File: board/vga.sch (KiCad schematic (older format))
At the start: 19 parts, among them P601 3-RCA

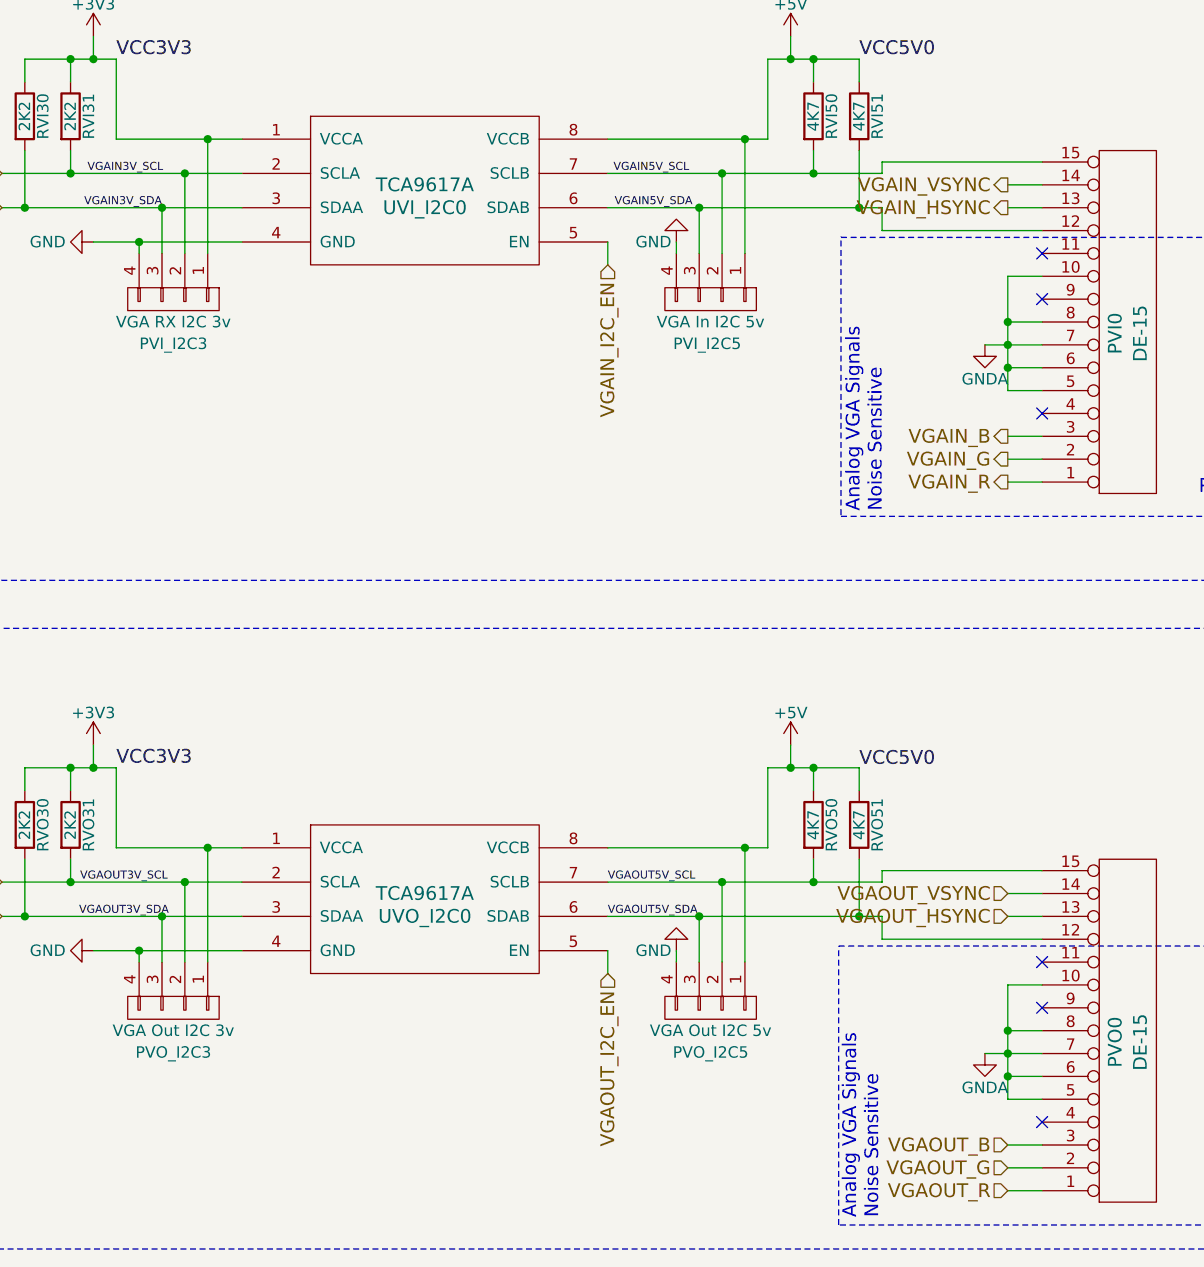
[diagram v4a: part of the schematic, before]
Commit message: Moving I2C enable pins to make IO1 a NC.
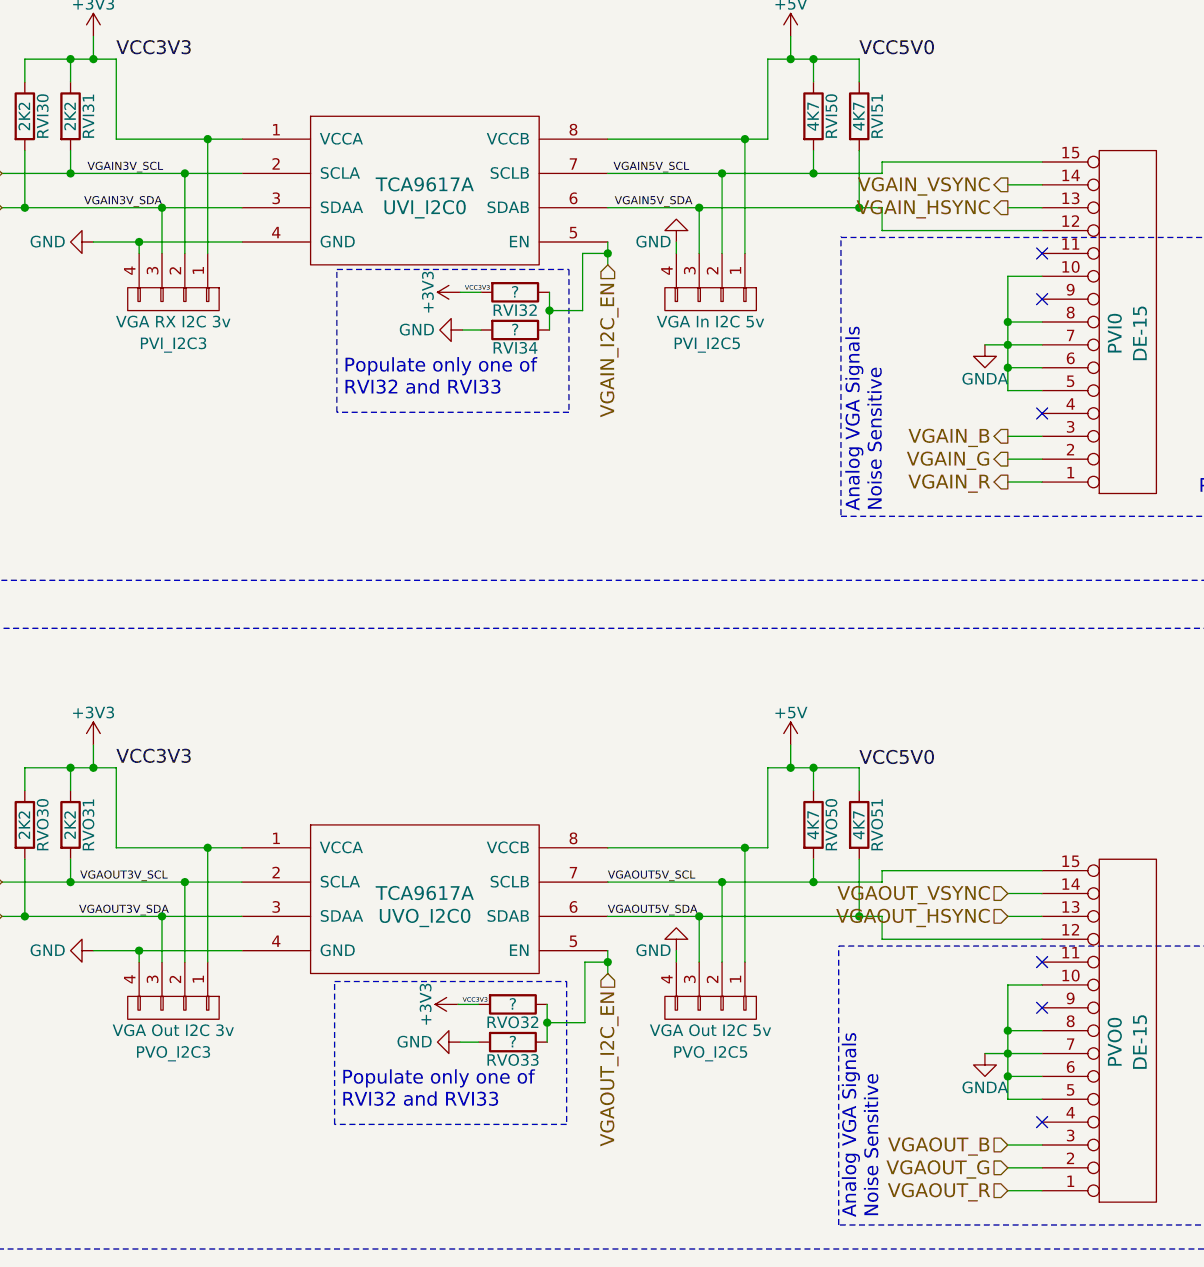
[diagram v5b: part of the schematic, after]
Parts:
- added RVI32, RVI34, RVO32, RVO33: ?, Resistors_SMD:R_0805_HandSoldering, symbol R
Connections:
- net +3V3: now also RVI32.2, RVO32.2
- net GND: now also RVI34.2, RVO33.2
- net VGAIN_I2C_EN: now also RVI32.1, RVI34.1
- net VGAOUT_I2C_EN: now also RVO32.1, RVO33.1
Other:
- note added: "Populate only one of \nRVI32 and RVI33"
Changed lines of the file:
@@
 Connection ~ 4600 5050
 Wire Wire Line
-	4600 5250 4600 5050
+	4600 5050 4600 5250
 Connection ~ 4700 4900
 Wire Wire Line
-	4700 5250 4700 4900
+	4700 4900 4700 5250
 Connection ~ 4800 4750
 Wire Wire Line
@@
 Connection ~ 4600 1950
 Wire Wire Line
-	4600 2150 4600 1950
+	4600 1950 4600 2150
 Connection ~ 4700 1800
 Wire Wire Line
-	4700 2150 4700 1800
+	4700 1800 4700 2150
 Connection ~ 4800 1650
 Wire Wire Line
@@
 	7650 1700 7650 1950
 Wire Wire Line
-	7750 1950 6550 1950
-Wire Wire Line
-	7750 1800 6550 1800
+	6550 1950 7750 1950
+Wire Wire Line
+	6550 1800 7750 1800
 Connection ~ 4000 1950
 Wire Wire Line
@@
 	4200 1400 4200 1300
 Wire Wire Line
-	7750 2050 7750 1950
-Wire Wire Line
-	7750 1750 7750 1800
+	7750 1950 7750 2050
+Wire Wire Line
+	7750 1800 7750 1750
 Connection ~ 8300 2450
 Connection ~ 8300 2650
@@
 	8300 2250 8300 2750
 Wire Wire Line
-	8450 2050 7750 2050
-Wire Wire Line
-	8450 1750 7750 1750
+	7750 2050 8450 2050
+Wire Wire Line
+	7750 1750 8450 1750
 Wire Wire Line
 	8450 2250 8300 2250
@@
 	7650 4800 7650 5050
 Wire Wire Line
-	7750 5050 6550 5050
-Wire Wire Line
-	7750 4900 6550 4900
+	6550 5050 7750 5050
+Wire Wire Line
+	6550 4900 7750 4900
 Connection ~ 4000 5050
 Wire Wire Line
@@
 	4200 4500 4200 4400
 Wire Wire Line
-	7750 5150 7750 5050
-Wire Wire Line
-	7750 4850 7750 4900
+	7750 5050 7750 5150
+Wire Wire Line
+	7750 4900 7750 4850
 Connection ~ 8300 5550
 Connection ~ 8300 5750
@@
 	8300 5350 8300 5850
 Wire Wire Line
-	8450 5150 7750 5150
-Wire Wire Line
-	8450 4850 7750 4850
+	7750 5150 8450 5150
+Wire Wire Line
+	7750 4850 8450 4850
 Wire Wire Line
 	8450 5350 8300 5350
@@
 Wire Notes Line
 	2755 2600 740  2600
+$Comp
+L R RVI32
+U 1 1 57A40937
+P 6145 2320
+F 0 "RVI32" V 6225 2320 50  0000 C CNN
+F 1 "?" V 6145 2320 50  0000 C CNN
+F 2 "Resistors_SMD:R_0805_HandSoldering" V 6075 2320 30  0001 C CNN
+F 3 "" H 6145 2320 30  0000 C CNN
+	1    6145 2320
+	0    1    1    0
+$EndComp
+$Comp
+L R RVI34
+U 1 1 57A40A93
+P 6145 2485
+F 0 "RVI34" V 6225 2485 50  0000 C CNN
+F 1 "?" V 6145 2485 50  0000 C CNN
+F 2 "Resistors_SMD:R_0805_HandSoldering" V 6075 2485 30  0001 C CNN
+F 3 "" H 6145 2485 30  0000 C CNN
+	1    6145 2485
+	0    1    1    0
+$EndComp
+Wire Wire Line
+	6295 2320 6295 2485
+Wire Wire Line
+	6295 2400 6440 2400
+Wire Wire Line
+	6440 2400 6440 2150
+Wire Wire Line
+	6440 2150 6550 2150
+Connection ~ 6550 2150
+Connection ~ 6295 2400
+$Comp
+L +3V3 #PWR?
+U 1 1 57A40F97
+P 5905 2320
+F 0 "#PWR?" H 5905 2170 50  0001 C CNN
+F 1 "+3V3" H 5905 2460 50  0000 C CNN
+F 2 "" H 5905 2320 60  0000 C CNN
+F 3 "" H 5905 2320 60  0000 C CNN
+	1    5905 2320
+	0    -1   -1   0
+$EndComp
+Text Label 5925 2320 0    20   ~ 0
+VCC3V3
+$Comp
+L GND #PWR?
+U 1 1 57A411C9
+P 5915 2485
+F 0 "#PWR?" H 5915 2235 50  0001 C CNN
+F 1 "GND" V 5915 2285 50  0000 C CNN
+F 2 "" H 5915 2485 60  0000 C CNN
+F 3 "" H 5915 2485 60  0000 C CNN
+	1    5915 2485
+	0    1    -1   0
+$EndComp
+Wire Wire Line
+	5995 2485 5915 2485
+Wire Wire Line
+	5905 2320 5995 2320
+Text Notes 5395 2780 0    60   ~ 0
+Populate only one of \nRVI32 and RVI33
+Wire Notes Line
+	5365 2220 6380 2220
+Wire Notes Line
+	6380 2220 6380 2845
+Wire Notes Line
+	6380 2845 5365 2845
+Wire Notes Line
+	5365 2845 5365 2230
+$Comp
+L R RVO32
+U 1 1 57A419BF
+P 6135 5435
+F 0 "RVO32" V 6215 5435 50  0000 C CNN
+F 1 "?" V 6135 5435 50  0000 C CNN
+F 2 "Resistors_SMD:R_0805_HandSoldering" V 6065 5435 30  0001 C CNN
+F 3 "" H 6135 5435 30  0000 C CNN
+	1    6135 5435
+	0    1    1    0
+$EndComp
+$Comp
+L R RVO33
+U 1 1 57A419C5
+P 6135 5600
+F 0 "RVO33" V 6215 5600 50  0000 C CNN
+F 1 "?" V 6135 5600 50  0000 C CNN
+F 2 "Resistors_SMD:R_0805_HandSoldering" V 6065 5600 30  0001 C CNN
+F 3 "" H 6135 5600 30  0000 C CNN
+	1    6135 5600
+	0    1    1    0
+$EndComp
+Wire Wire Line
+	6285 5435 6285 5600
+Wire Wire Line
+	6285 5515 6450 5515
+Connection ~ 6285 5515
+$Comp
+L +3V3 #PWR?
+U 1 1 57A419CF
+P 5895 5435
+F 0 "#PWR?" H 5895 5285 50  0001 C CNN
+F 1 "+3V3" H 5895 5575 50  0000 C CNN
+F 2 "" H 5895 5435 60  0000 C CNN
+F 3 "" H 5895 5435 60  0000 C CNN
+	1    5895 5435
+	0    -1   -1   0
+$EndComp
+Text Label 5915 5435 0    20   ~ 0
+VCC3V3
+$Comp
+L GND #PWR?
+U 1 1 57A419D6
+P 5905 5600
+F 0 "#PWR?" H 5905 5350 50  0001 C CNN
+F 1 "GND" V 5905 5400 50  0000 C CNN
+F 2 "" H 5905 5600 60  0000 C CNN
+F 3 "" H 5905 5600 60  0000 C CNN
+	1    5905 5600
+	0    1    -1   0
+$EndComp
+Wire Wire Line
+	5985 5600 5905 5600
+Wire Wire Line
+	5895 5435 5985 5435
+Text Notes 5385 5895 0    60   ~ 0
+Populate only one of \nRVI32 and RVI33
+Wire Notes Line
+	5355 5335 6370 5335
+Wire Notes Line
+	6370 5335 6370 5960
+Wire Notes Line
+	6370 5960 5355 5960
+Wire Notes Line
+	5355 5960 5355 5345
+Wire Wire Line
+	6450 5515 6450 5250
+Wire Wire Line
+	6450 5250 6550 5250
+Connection ~ 6550 5250
 $EndSCHEMATC

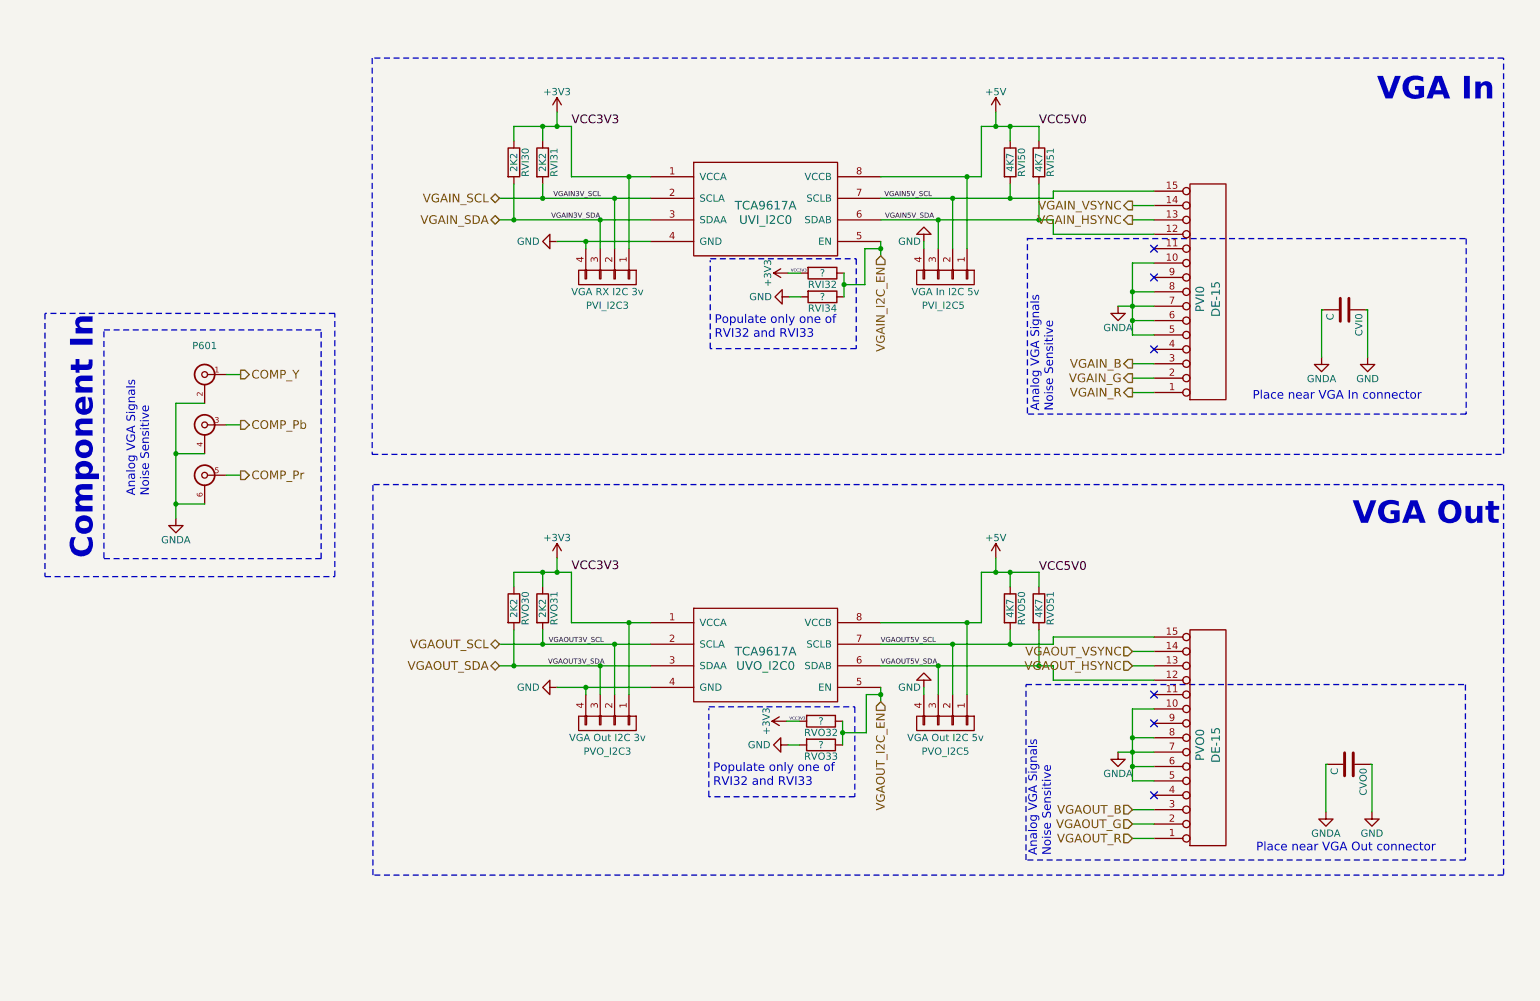
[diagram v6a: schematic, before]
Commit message: Added ESD protection to video inputs Changed level shifter to TPSDS019 because it also contains ESD protection
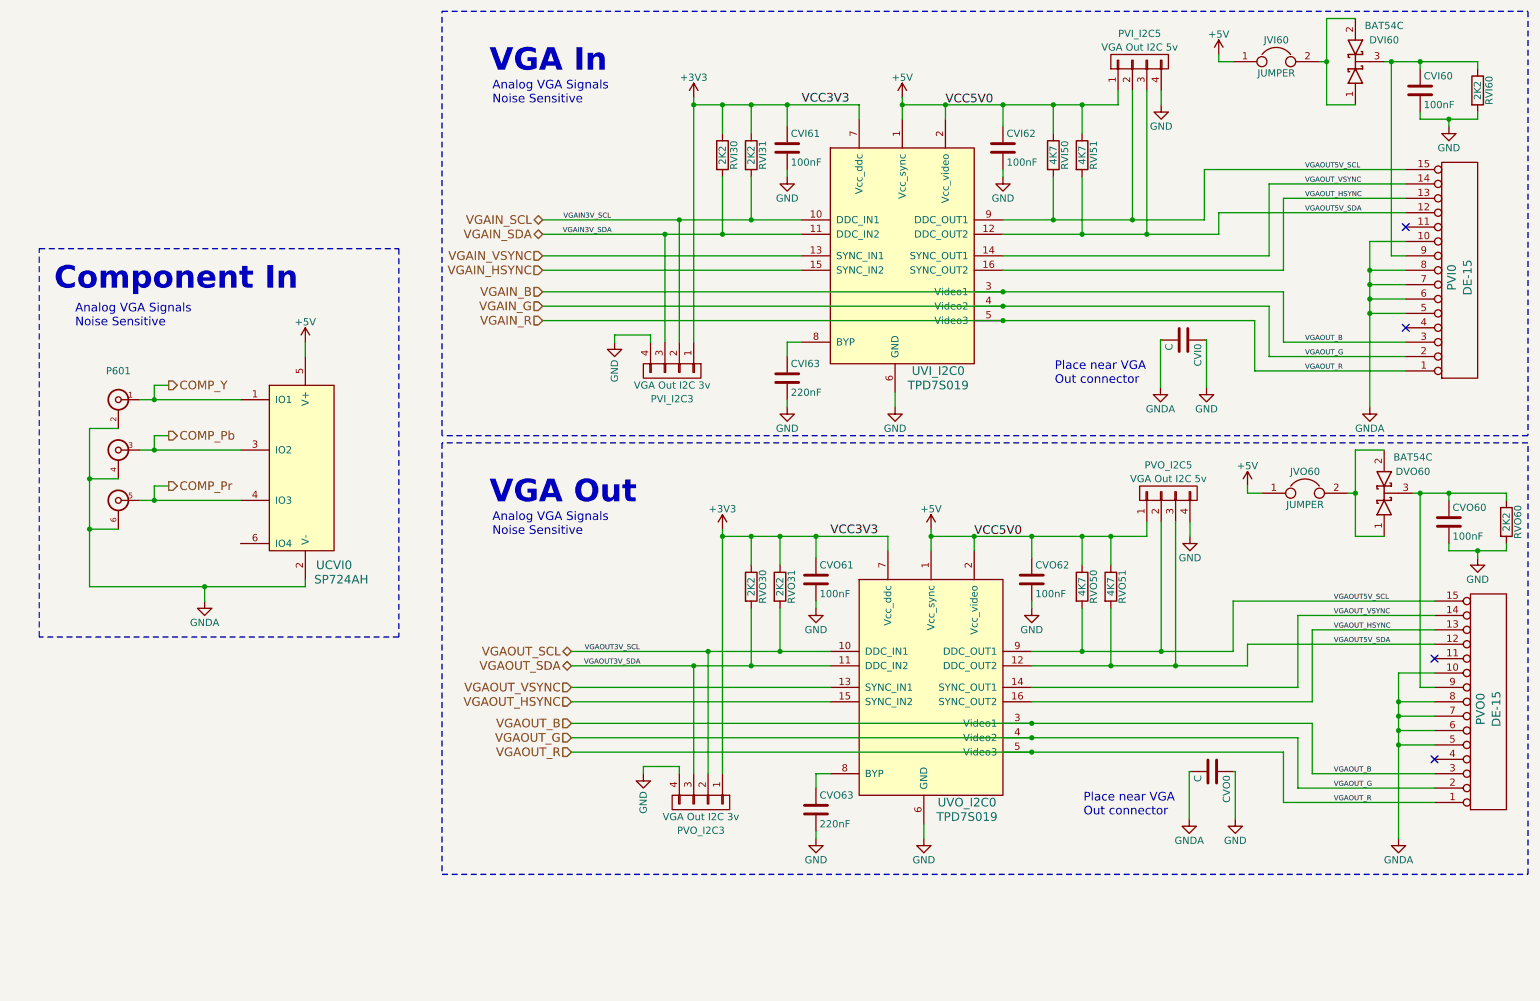
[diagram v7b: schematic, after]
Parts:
- removed RVI32, RVI34, RVO32, RVO33: ?, Resistors_SMD:R_0805_HandSoldering, symbol R
- removed UVI_I2C0, UVO_I2C0: TCA9617A, Housings_SSOP:MSOP-8_3x3mm_Pitch0.65mm, symbol TCA9617A
- added CVI60, CVI61, CVI62, CVO60, CVO61, CVO62: 100nF, symbol C
- added CVI63, CVO63: 220nF, symbol C
- added DVI60, DVO60: BAT54C, symbol D_Schottky_x2_KCom_AAK
- added JVI60, JVO60: JUMPER, symbol JUMPER
- added RVI60, RVO60: 2K2, Resistors_SMD:R_0805_HandSoldering, symbol R
- added UCVI0: SP724AH, SOT23-6, symbol SP724AH
- added UVI_I2C0, UVO_I2C0: TPD7S019, SSOP-16, symbol TPD7S019
- PVI_I2C3: value VGA RX I2C 3v -> VGA Out I2C 3v
- PVI_I2C5: value VGA In I2C 5v -> VGA Out I2C 5v
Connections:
- net VGAIN5V_SCL is gone; now on net VGAOUT5V_SCL: PVI0.15 (P15), PVI_I2C5.2 (P2), RVI50.2
- net VGAIN5V_SDA is gone; now on net VGAOUT5V_SDA: PVI0.12 (P12), PVI_I2C5.3 (P3), RVI51.2
- net VGAOUT_B is gone; now on net VGAIN_B: PVO0.3 (P3)
- net VGAOUT_G is gone; now on net VGAIN_G: PVO0.2 (P2)
- net VGAOUT_R is gone; now on net VGAIN_R: PVO0.1 (P1)
- net +3V3: now also CVI61.1, CVO61.1, UVI_I2C0.7 (Vcc_ddc), UVO_I2C0.7 (Vcc_ddc)
- net +5V: now also CVI62.1, CVO62.1, JVI60.1, JVO60.1, UCVI0.5 (V+), UVI_I2C0.1 (Vcc_sync), UVI_I2C0.2 (Vcc_video), UVO_I2C0.1 (Vcc_sync), UVO_I2C0.2 (Vcc_video)
- net COMP_Pb: now also UCVI0.3 (IO2)
- net COMP_Pr: now also UCVI0.4 (IO3)
- net COMP_Y: now also UCVI0.1 (IO1)
- net GND: now also CVI60.2, CVI61.2, CVI62.2, CVI63.2, CVO60.2, CVO61.2, CVO62.2, CVO63.2, RVI60.2, RVO60.2, UVI_I2C0.6 (GND), UVO_I2C0.6 (GND)
- net GNDA: now also UCVI0.2 (V-)
- net VGAIN_B: now also UVI_I2C0.3 (Video1), UVO_I2C0.3 (Video1)
- net VGAIN_G: now also UVI_I2C0.4 (Video2), UVO_I2C0.4 (Video2)
- net VGAIN_HSYNC: now also UVI_I2C0.15 (SYNC_IN2); no longer PVI0.13 (P13)
- net VGAIN_R: now also UVI_I2C0.5 (Video3), UVO_I2C0.5 (Video3)
- net VGAIN_SCL: now also UVI_I2C0.10 (DDC_IN1)
- net VGAIN_SDA: now also UVI_I2C0.11 (DDC_IN2)
- net VGAIN_VSYNC: now also UVI_I2C0.13 (SYNC_IN1); no longer PVI0.14 (P14)
- net VGAOUT5V_SCL: now also UVI_I2C0.9 (DDC_OUT1), UVO_I2C0.9 (DDC_OUT1)
- net VGAOUT5V_SDA: now also UVI_I2C0.12 (DDC_OUT2), UVO_I2C0.12 (DDC_OUT2)
- net VGAOUT_HSYNC: now also PVI0.13 (P13), UVI_I2C0.16 (SYNC_OUT2), UVO_I2C0.15 (SYNC_IN2), UVO_I2C0.16 (SYNC_OUT2)
- net VGAOUT_SCL: now also UVO_I2C0.10 (DDC_IN1)
- net VGAOUT_SDA: now also UVO_I2C0.11 (DDC_IN2)
- net VGAOUT_VSYNC: now also PVI0.14 (P14), UVI_I2C0.14 (SYNC_OUT1), UVO_I2C0.13 (SYNC_IN1), UVO_I2C0.14 (SYNC_OUT1)
- net at PVO0.9 (P9): now also CVO60.1, DVO60.3 (K), RVO60.1
- net at PVI0.9 (P9): now also CVI60.1, DVI60.3 (K), RVI60.1
- new net: DVO60.1 (A), DVO60.2 (A), JVO60.2
- new net: CVO63.1, UVO_I2C0.8 (BYP)
- new net: DVI60.1 (A), DVI60.2 (A), JVI60.2
- new net: CVI63.1, UVI_I2C0.8 (BYP)
- no-connect marks 6 -> 4
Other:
- note added: "Place near VGA\nOut connector"
- note removed: "Place near VGA In connector"
- note removed: "Place near VGA Out connector"
- note removed: "Populate only one of \nRVI32 and RVI33"
- moved on the sheet: CVO0, P601, PVO0, PVO_I2C3, PVO_I2C5, RVO30, RVO31, RVO50, RVO51
